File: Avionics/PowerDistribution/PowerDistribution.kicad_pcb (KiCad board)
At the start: 4 copper layers, 90.2 x 96 mm, 170 parts, among them J1 Conn_02x26_Odd_Even, J10 Conn_01x02, J11 Conn_01x04, J12 Conn_01x04, J13 Conn_01x04, J14 Conn_01x02, J15 Conn_01x02, J2 Conn_02x26_Odd_Even, J3 Conn_01x02, J4 Conn_01x02, J5 Conn_01x02, J6 Conn_01x02, J7 USB_C_Receptacle_USB2.0_14P, J8 Conn_01x02, J9 Conn_01x02, Q1 BC848ALT1G, Q2 IRLML2803PBFCT, Q3 IRLML2803PBFCT, U1 LT8610, U16 INA219AxD, U17 INA219AxD, U18 INA219AxD, U19 LT3652EDD, U2 LT8610, U21 INA219AxD, U6 LT8610

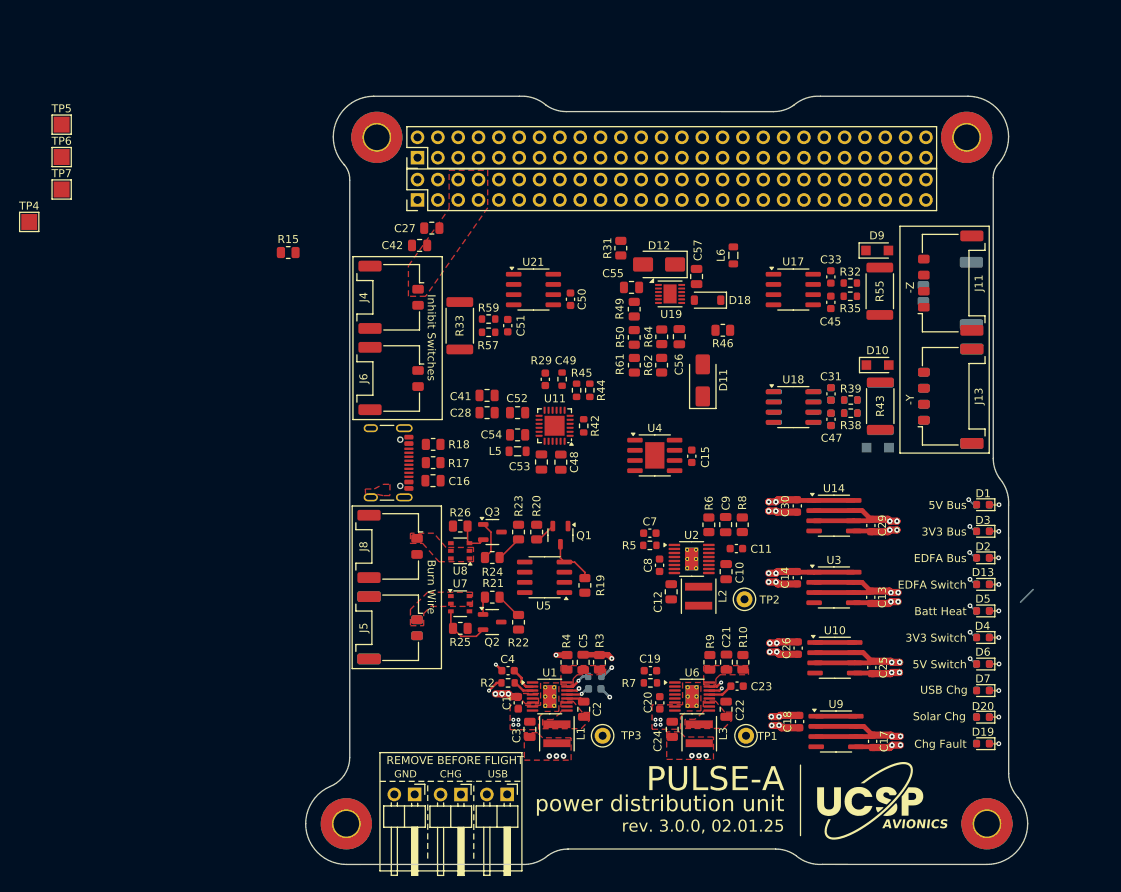
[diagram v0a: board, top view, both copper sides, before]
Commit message: feat: PDU 3.0.0 & laser driving basics
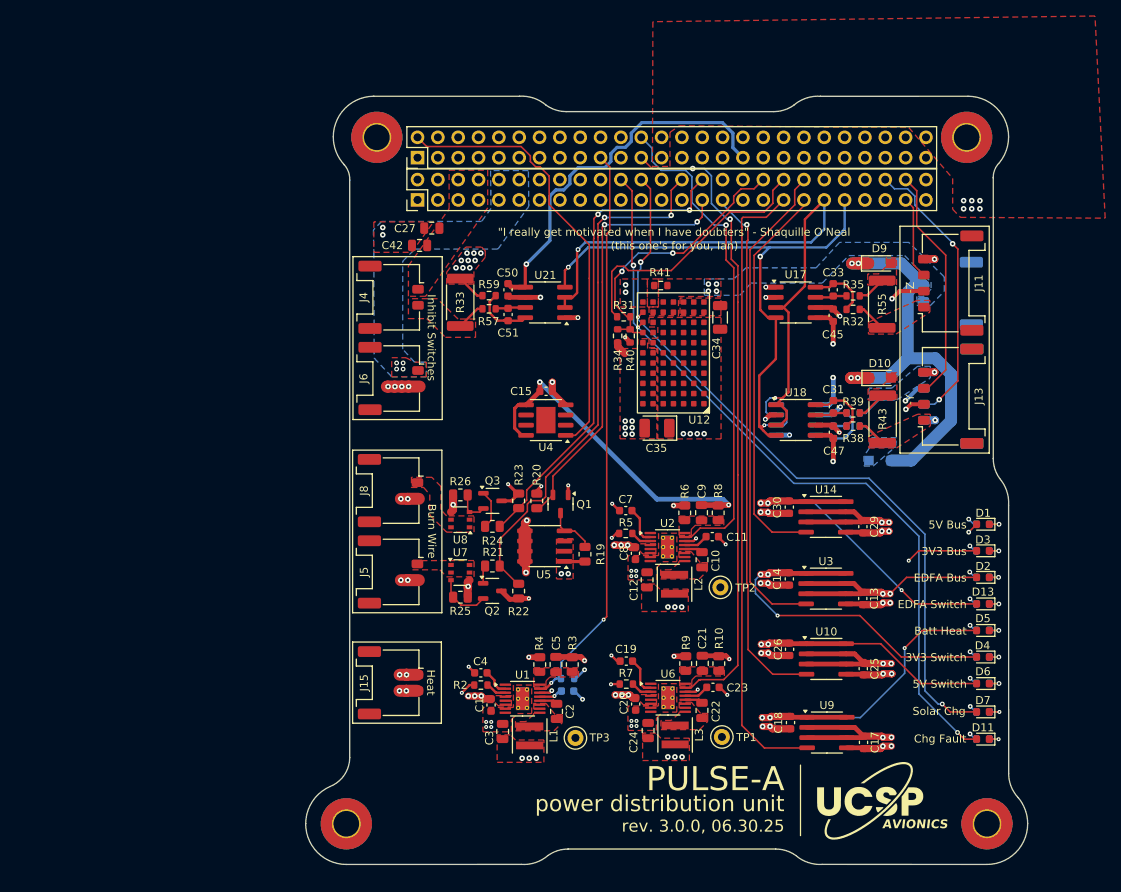
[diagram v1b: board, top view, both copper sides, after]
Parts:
- removed C16: 4.7uF, Capacitor_SMD:C_0805_2012Metric
- removed C28, C41: 20uF, Capacitor_SMD:C_0805_2012Metric
- removed C48, C57: 1uF, Capacitor_SMD:C_0805_2012Metric
- removed C49: 4.7uF, Capacitor_SMD:C_0603_1608Metric
- removed C52, C53, C55, C56: 10uF, Capacitor_SMD:C_0805_2012Metric
- removed C54: 47nF, Capacitor_SMD:C_0805_2012Metric
- removed D12: CMSH3-40MA, Diode_SMD:D_SMA
- removed D18: 1N4148, Diode_SMD:D_SOD-123
- removed D19, D20: 150060RS75000, LED_SMD:LED_0603_1608Metric
- removed J10, J14, J9: Conn_01x02, Connector_PinHeader_2.54mm:PinHeader_1x02_P2.54mm_Horizontal
- removed J7: USB_C_Receptacle_USB2.0_14P, Connector_USB:USB_C_Receptacle_GCT_USB4105-xx-A_16P_TopMnt_Horizontal
- removed L5: AIML-0805-1RO, Inductor_SMD:L_0805_2012Metric
- removed L6: TBD, Inductor_SMD:L_0805_2012Metric
- removed R15: 0, Resistor_SMD:R_0805_2012Metric
- removed R18: 5.1k, Resistor_SMD:R_0805_2012Metric
- removed R29: 3.16k, Resistor_SMD:R_0603_1608Metric
- removed R42: 5.23k, Resistor_SMD:R_0603_1608Metric
- removed R44: 30.1k, Resistor_SMD:R_0603_1608Metric
- removed R45: 10k, Resistor_SMD:R_0603_1608Metric
- removed R46: 165m, Resistor_SMD:R_0805_2012Metric
- removed R49, R50, R61, R62, R64: TBD, Resistor_SMD:R_0805_2012Metric
- removed R60, R65: TBD, Resistor_SMD:R_0603_1608Metric
- removed TP4, TP5, TP6, TP7: ~, TestPoint:TestPoint_Pad_2.0x2.0mm
- removed U11: ~, Package_DFN_QFN:VQFN-24-1EP_4x4mm_P0.5mm_EP2.5x2.5mm
- removed U19: LT3652EDD, Package_DFN_QFN:DFN-12-1EP_3x3mm_P0.45mm_EP1.65x2.38mm
- added C34: 4.7uF, Capacitor_SMD:C_1206_3216Metric, F.Cu at (218.8, 77.6)
- added C35: 4.7uF, Capacitor_Tantalum_SMD:CP_EIA-3528-12_Kemet-T, F.Cu at (210.9, 91.4)
- added R34: 549k, Resistor_SMD:R_0603_1608Metric, F.Cu at (206.0, 79.9)
- added R40: 459k, Resistor_SMD:R_0603_1608Metric, F.Cu at (207.5, 79.9)
- added R41: 0, Resistor_SMD:R_0603_1608Metric, F.Cu at (211.4, 73.6)
- added U12: LTM8062AIV-PBF, PDU:LGA-77, F.Cu at (212.9, 82.0)
- D11: value CMSH3-40MA -> 150060VS75000; footprint Diode_SMD:D_SMA -> LED_SMD:LED_0603_1608Metric
- J15: moved to F.Cu
- R16: value 10k -> 150
- R17: value 5.1k -> 150; footprint Resistor_SMD:R_0805_2012Metric -> Resistor_SMD:R_0603_1608Metric; moved to B.Cu
- R31: value 0 -> 549k; footprint Resistor_SMD:R_0805_2012Metric -> Resistor_SMD:R_0603_1608Metric
- moved R17 76.9 mm to (251.6, 130.2)
- moved D11 56.8 mm to (251.6, 130.2), turned to 180 degrees
- moved C15 19.9 mm to (197.0, 86.8), turned to 180 degrees
- moved U4 14.3 mm to (197.0, 90.4), turned to 180 degrees
- moved R31 8.57 mm to (206.7, 77.5), turned to 0 degrees
- moved C50 7.89 mm to (192.3, 74.1), turned to 90 degrees
- moved J5 6.97 mm to (177.6, 109.4)
- moved J8 6.97 mm to (177.6, 99.2)
- moved J15 6.87 mm to (177.6, 123.2), turned to -90 degrees
- moved C7 4.12 mm to (207.0, 101.7)
- moved Q2 3.89 mm to (190.3, 111.7)
- moved R19 3.89 mm to (201.9, 107.1)
- moved R20 3.89 mm to (195.9, 100.5)
- moved R22 3.89 mm to (193.6, 111.8)
- moved R23 3.89 mm to (193.6, 100.5)
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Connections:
- C1 pad 2: V_BATT -> VBATT
- C20 pad 1: V_BATT -> VBATT
- C27 pad 2: /BATT_RAW -> /VBATT_IN
- C42 pad 2: /BATT_RAW -> /VBATT_IN
- C8 pad 2: V_BATT -> VBATT
- D11 pad 1: V_BATT -> Net-(D11-K)
- D11 pad 2: /OUT -> /FAULT
- D7 pad 2: Net-(D7-A) -> /CHRG
- J1 pad 13: KAPTON_EN -> unconnected-(J1-Pin_13-Pad13)
- J1 pad 15: /EDFA_EN -> unconnected-(J1-Pin_15-Pad15)
- J1 pad 21: 5V_S -> unconnected-(J1-Pin_21-Pad21)
- J1 pad 26: /SHDN -> unconnected-(J1-Pin_26-Pad26)
- J1 pad 27: /PERIPH_EN -> unconnected-(J1-Pin_27-Pad27)
- J1 pad 34: unconnected-(J1-Pin_34-Pad34) -> 3V3_S
- J1 pad 36: unconnected-(J1-Pin_36-Pad36) -> /ADJ
- J1 pad 37: unconnected-(J1-Pin_37-Pad37) -> KAPTON_EN
- J1 pad 38: unconnected-(J1-Pin_38-Pad38) -> /BATT_THERM_R
- J1 pad 39: unconnected-(J1-Pin_39-Pad39) -> 3V3_S_EN
- J1 pad 40: unconnected-(J1-Pin_40-Pad40) -> EDFA_5V_EN
- J1 pad 42: unconnected-(J1-Pin_42-Pad42) -> EDFA_5V_S
- J1 pad 44: unconnected-(J1-Pin_44-Pad44) -> EDFA_5V_S
- J1 pad 45: unconnected-(J1-Pin_45-Pad45) -> 5V_S
- J1 pad 46: unconnected-(J1-Pin_46-Pad46) -> 5V_S
- J1 pad 47: /PERIPH_PWR -> unconnected-(J1-Pin_47-Pad47)
- J1 pad 5: /RAW_BATT -> /VBATT_IN
- J1 pad 6: /RAW_BATT -> /VBATT_IN
- J1 pad 7: /RAW_BATT -> /VBATT_IN
- J1 pad 8: /RAW_BATT -> /VBATT_IN
- J11 pad 2: /3V3_BUS -> 3V3
- J12 pad 2: /3V3_BUS -> 3V3
- J13 pad 2: /3V3_BUS -> 3V3
- J2 pad 21: EDFA_5V_S -> unconnected-(J2-Pin_21-Pad21)
- J2 pad 22: EDFA_5V_S -> unconnected-(J2-Pin_22-Pad22)
- J2 pad 23: /5V_BUS_STAT -> 5V_STAT
- J2 pad 24: /3V3_BUS_STAT -> 3V3_STAT
- J2 pad 33: unconnected-(J2-Pin_33-Pad33) -> 3V3_S
- J2 pad 45: V_BATT -> VBATT
- J2 pad 46: V_BATT -> VBATT
- J2 pad 48: V_BATT -> VBATT
- J4 pad 1: /BATT_RAW -> /VBATT_IN
- R16 pad 1: Net-(D7-A) -> GND
- R16 pad 2: /REGN -> Net-(D7-K)
- R17 pad 1: Net-(J7-CC2) -> GND
- R17 pad 2: GND_REF -> Net-(D11-K)
- R19 pad 1: V_BATT -> VBATT
- R31 pad 1: GNDA -> /BATT_THERM_R
- R31 pad 2: GND -> /ADJ
- R33 pad 2: V_BATT -> VBATT
- R59 pad 1: V_BATT -> VBATT
- U1 pad 4: V_BATT -> VBATT
- U1 pad 5: V_BATT -> VBATT
- U1 pad 6: V_BATT -> VBATT
- U16 pad 2: SDA -> SCL
- U17 pad 2: SDA -> GND
- U18 pad 1: GND -> SDA
- U18 pad 2: SDA -> GND
- U2 pad 4: V_BATT -> VBATT
- U2 pad 5: V_BATT -> VBATT
- U2 pad 6: V_BATT -> VBATT
- U5 pad 1: V_BATT -> VBATT
- U5 pad 2: V_BATT -> VBATT
- U5 pad 3: V_BATT -> VBATT
- U6 pad 4: V_BATT -> VBATT
- U6 pad 5: V_BATT -> VBATT
- U6 pad 6: V_BATT -> VBATT
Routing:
- net /FAULT: track 0.00 -> 95.4 mm, vias 0 -> 3
- net 3V3_S: track 10.8 -> 105.4 mm, vias 2 -> 7
- net /CHRG: track 0.00 -> 93.5 mm, vias 0 -> 3
- net SDA: track 0.00 -> 82.8 mm, vias 0 -> 2
- net KAPTON_EN: track 0.00 -> 79.0 mm
- net 5V_STAT: track 1.70 -> 80.2 mm, vias 1 -> 2
- net SCL: track 0.00 -> 77.1 mm, vias 0 -> 3
- net EDFA_5V_STAT: track 3.20 -> 71.2 mm, vias 1 -> 2
- net 5V_S_EN: track 0.00 -> 66.5 mm, vias 0 -> 1
- net GND: track 50.8 -> 115.5 mm, vias 35 -> 83
- net ENAB_BURN_1: track 3.28 -> 66.5 mm, vias 0 -> 2
- net 3V3: track 18.1 -> 81.2 mm, vias 2 -> 12
- net 3V3_STAT: track 0.00 -> 62.2 mm, vias 0 -> 1
- net EDFA_5V_EN: track 0.00 -> 61.2 mm
- net ENAB_BURN_2: track 3.30 -> 60.2 mm, vias 0 -> 2
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- added copper zone on F.Cu, net /BATT_CS
- added copper zone on F.Cu, net /CHARGE_VIN
- added copper zone on F.Cu, net /FB_2
- added copper zone on B.Cu, net /SOLAR_IN_+Y
- added copper zone on F.Cu, net /SOLAR_IN_-Y
- added copper zone on F.Cu, net /SOLAR_IN_-Z
- added copper zone on B.Cu, net /SOLAR_PRE_MPPT
- added copper zone on F.Cu, net /SOLAR_PRE_MPPT
- added copper zone on F.Cu, net /SW_2
- added copper zone on F.Cu, net /VBATT_IN
- added copper zone on F.Cu, net /VIN_REG
- added copper zone on F.Cu, net /sol_1_diode
- added copper zone on B.Cu, net /sol_2_diode
- added copper zone on F.Cu, net /sol_3_diode
- added copper zone on F.Cu, net 3V3
- added copper zone on B.Cu, net GND_REF
- added copper zone on F.Cu, net GND_REF
- added copper zone on F.Cu, net VBATT
- added copper zone on In2.Cu, net VBATT
- removed copper zone on F.Cu, net /BATT_RAW
- removed copper zone on F.Cu, net /V_BUS
- removed copper zone on F.Cu, net V_BATT
- removed copper zone on In2.Cu, net V_BATT
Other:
- board text added: "(this one's for you, Ian)"
- board text added: "rev. 3.0.0, 06.30.25"
- board text added: "{dblquote}I really get motivated when I have doubters{dblquote} - Shaquille O'Neal"
- board text removed: "CHG"
- board text removed: "GND"
- board text removed: "REMOVE BEFORE FLIGHT"
- board text removed: "USB"
- board text removed: "USB Chg"
- board text removed: "rev. 3.0.0, 02.01.25"
